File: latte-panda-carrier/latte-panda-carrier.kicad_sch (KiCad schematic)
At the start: 6 parts

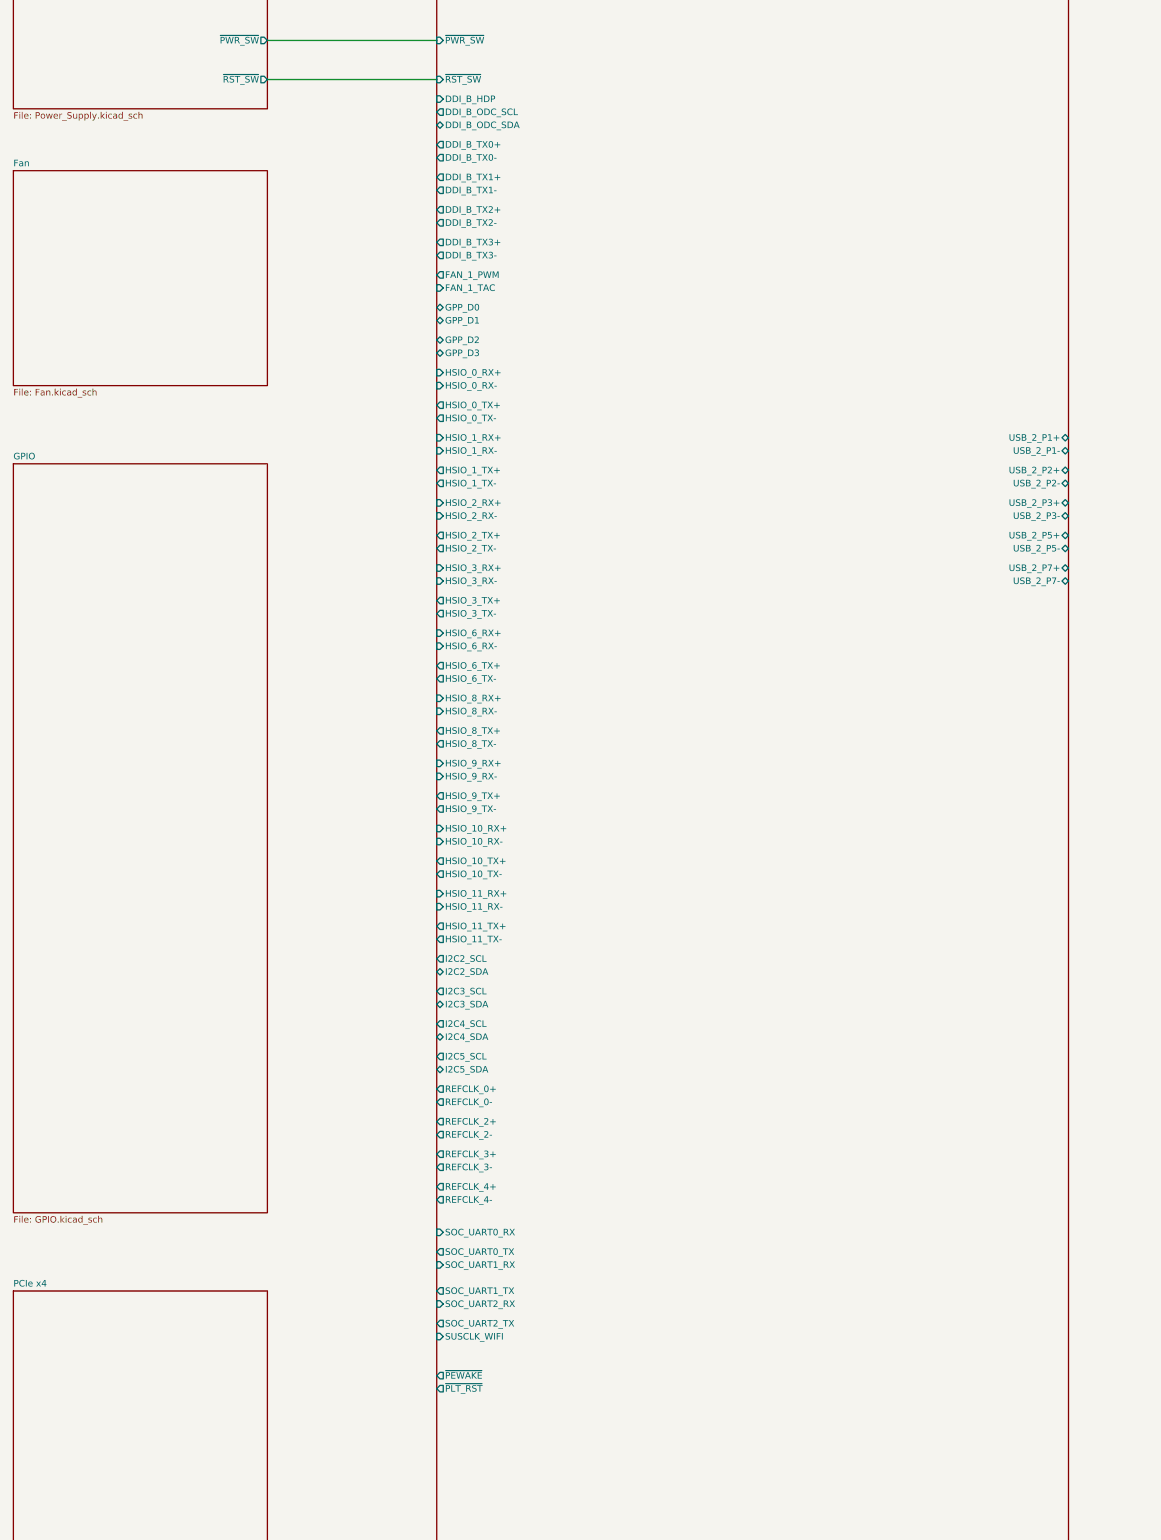
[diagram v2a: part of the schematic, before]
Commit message: 120.2
Wire CPU fan on root sheet and fix 2 power net name problems (+3V3 symbols
changed to +3.3V)
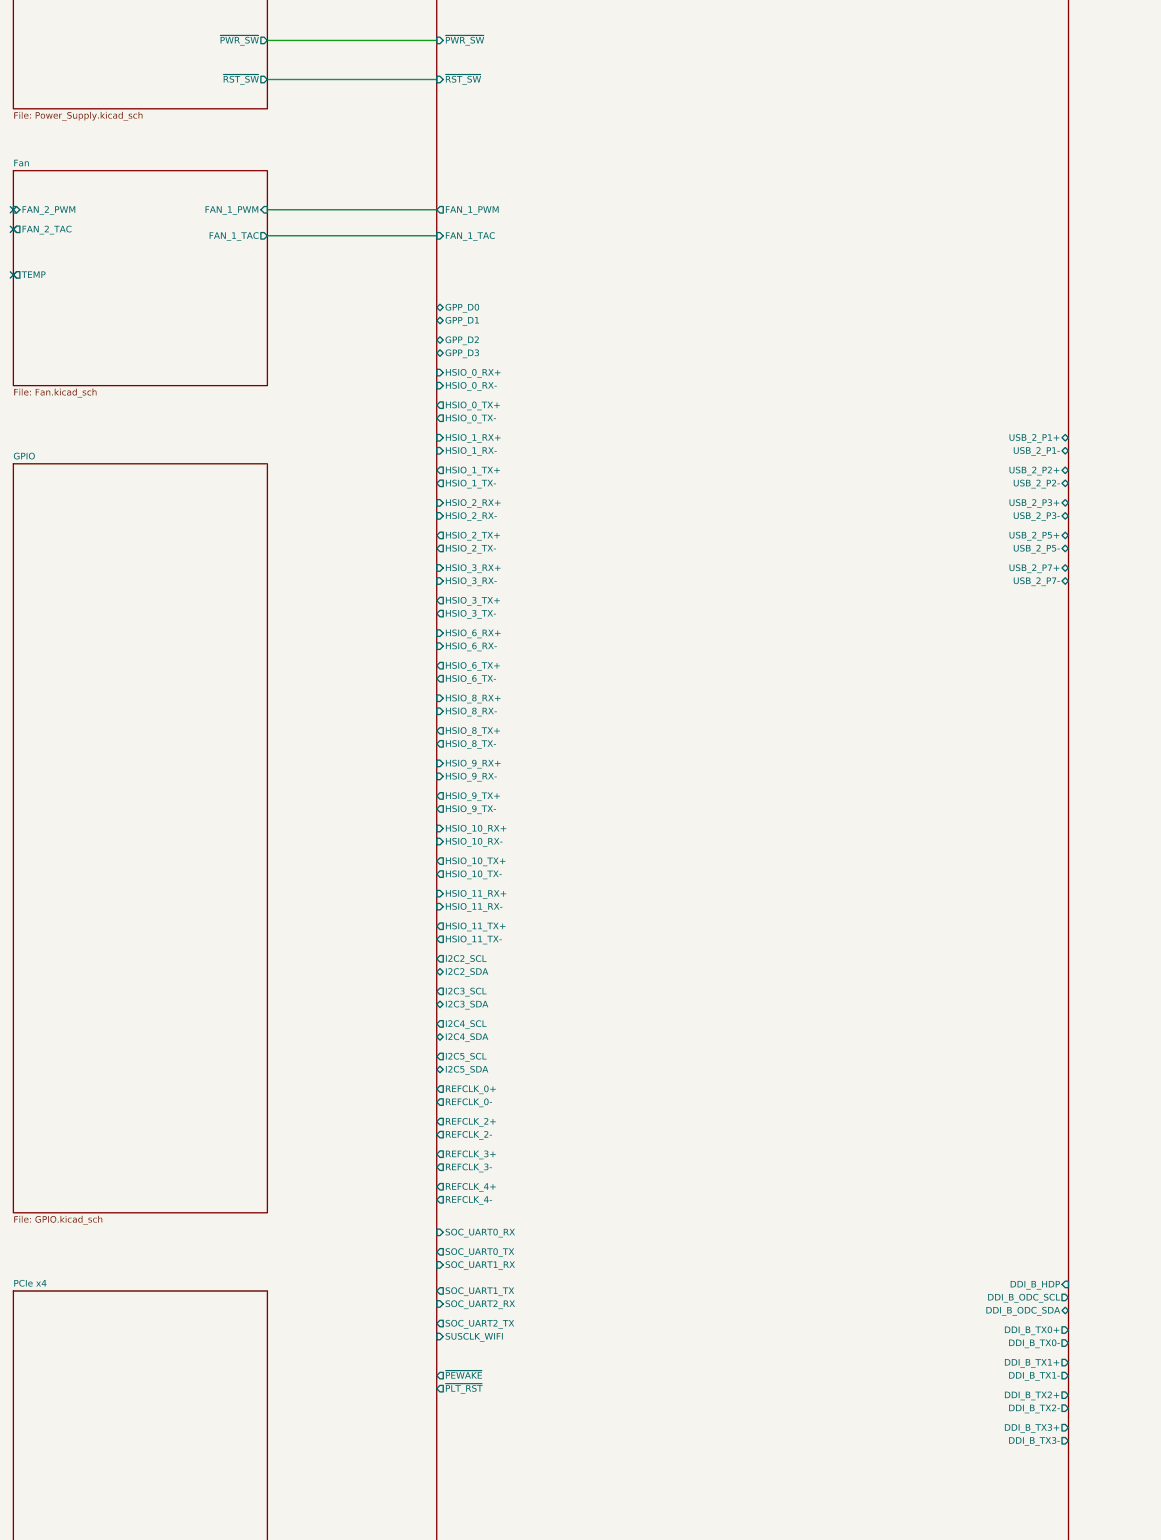
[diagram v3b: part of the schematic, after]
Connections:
- no-connect marks 0 -> 3
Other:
- sheet Fan ports: added FAN_1_PWM, FAN_1_TAC, FAN_2_PWM, FAN_2_TAC, TEMP; removed none
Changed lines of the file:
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@@
 		(rev "1.0")
+	)
+	(no_connect
+		(at 134.62 97.79)
+	)
+	(no_connect
+		(at 134.62 101.6)
+	)
+	(no_connect
+		(at 134.62 110.49)
 	)
 	(wire
@@
 		(pts
 			(xy 184.15 72.39) (xy 217.17 72.39)
+		)
+		(stroke
+			(width 0)
+			(type default)
+		)
+	)
+	(wire
+		(pts
+			(xy 184.15 97.79) (xy 217.17 97.79)
+		)
+		(stroke
+			(width 0)
+			(type default)
+		)
+	)
+	(wire
+		(pts
+			(xy 184.15 102.87) (xy 217.17 102.87)
 		)
 		(stroke
@@
 			)
 		)
+		(pin "FAN_1_PWM" input
+			(at 184.15 97.79 0)
+			(effects
+				(font
+					(size 1.27 1.27)
+				)
+				(justify right)
+			)
+		)
+		(pin "FAN_1_TAC" output
+			(at 184.15 102.87 0)
+			(effects
+				(font
+					(size 1.27 1.27)
+				)
+				(justify right)
+			)
+		)
+		(pin "FAN_2_PWM" input
+			(at 134.62 97.79 180)
+			(effects
+				(font
+					(size 1.27 1.27)
+				)
+				(justify left)
+			)
+		)
+		(pin "FAN_2_TAC" output
+			(at 134.62 101.6 180)
+			(effects
+				(font
+					(size 1.27 1.27)
+				)
+				(justify left)
+			)
+		)
+		(pin "TEMP" output
+			(at 134.62 110.49 180)
+			(effects
+				(font
+					(size 1.27 1.27)
+				)
+				(justify left)
+			)
+		)
 		(instances
 			(project "latte-panda-carrier"
@@
 		)
 		(pin "DDI_B_HDP" input
-			(at 217.17 76.2 180)
-			(effects
-				(font
-					(size 1.27 1.27)
-				)
-				(justify left)
+			(at 340.36 307.34 0)
+			(effects
+				(font
+					(size 1.27 1.27)
+				)
+				(justify right)
 			)
 		)
 		(pin "DDI_B_ODC_SCL" output
-			(at 217.17 78.74 180)
-			(effects
-				(font
-					(size 1.27 1.27)
-				)
-				(justify left)
+			(at 340.36 309.88 0)
+			(effects
+				(font
+					(size 1.27 1.27)
+				)
+				(justify right)
 			)
 		)
 		(pin "DDI_B_ODC_SDA" bidirectional
-			(at 217.17 81.28 180)
-			(effects
-				(font
-					(size 1.27 1.27)
-				)
-				(justify left)
+			(at 340.36 312.42 0)
+			(effects
+				(font
+					(size 1.27 1.27)
+				)
+				(justify right)
 			)
 		)
 		(pin "DDI_B_TX0+" output
-			(at 217.17 85.09 180)
-			(effects
-				(font
-					(size 1.27 1.27)
-				)
-				(justify left)
+			(at 340.36 316.23 0)
+			(effects
+				(font
+					(size 1.27 1.27)
+				)
+				(justify right)
 			)
 		)
 		(pin "DDI_B_TX0-" output
-			(at 217.17 87.63 180)
-			(effects
-				(font
-					(size 1.27 1.27)
-				)
-				(justify left)
+			(at 340.36 318.77 0)
+			(effects
+				(font
+					(size 1.27 1.27)
+				)
+				(justify right)
 			)
 		)
 		(pin "DDI_B_TX1+" output
-			(at 217.17 91.44 180)
-			(effects
-				(font
-					(size 1.27 1.27)
-				)
-				(justify left)
+			(at 340.36 322.58 0)
+			(effects
+				(font
+					(size 1.27 1.27)
+				)
+				(justify right)
 			)
 		)
 		(pin "DDI_B_TX1-" output
-			(at 217.17 93.98 180)
-			(effects
-				(font
-					(size 1.27 1.27)
-				)
-				(justify left)
+			(at 340.36 325.12 0)
+			(effects
+				(font
+					(size 1.27 1.27)
+				)
+				(justify right)
 			)
 		)
 		(pin "DDI_B_TX2+" output
+			(at 340.36 328.93 0)
+			(effects
+				(font
+					(size 1.27 1.27)
+				)
+				(justify right)
+			)
+		)
+		(pin "DDI_B_TX2-" output
+			(at 340.36 331.47 0)
+			(effects
+				(font
+					(size 1.27 1.27)
+				)
+				(justify right)
+			)
+		)
+		(pin "DDI_B_TX3+" output
+			(at 340.36 335.28 0)
+			(effects
+				(font
+					(size 1.27 1.27)
+				)
+				(justify right)
+			)
+		)
+		(pin "DDI_B_TX3-" output
+			(at 340.36 337.82 0)
+			(effects
+				(font
+					(size 1.27 1.27)
+				)
+				(justify right)
+			)
+		)
+		(pin "FAN_1_PWM" output
 			(at 217.17 97.79 180)
 			(effects
@@
 			)
 		)
-		(pin "DDI_B_TX2-" output
-			(at 217.17 100.33 180)
-			(effects
-				(font
-					(size 1.27 1.27)
-				)
-				(justify left)
-			)
-		)
-		(pin "DDI_B_TX3+" output
-			(at 217.17 104.14 180)
-			(effects
-				(font
-					(size 1.27 1.27)
-				)
-				(justify left)
-			)
-		)
-		(pin "DDI_B_TX3-" output
-			(at 217.17 106.68 180)
-			(effects
-				(font
-					(size 1.27 1.27)
-				)
-				(justify left)
-			)
-		)
-		(pin "FAN_1_PWM" output
-			(at 217.17 110.49 180)
-			(effects
-				(font
-					(size 1.27 1.27)
-				)
-				(justify left)
-			)
-		)
 		(pin "FAN_1_TAC" input
-			(at 217.17 113.03 180)
-			(effects
-				(font
+			(at 217.17 102.87 180)
+			(effects
+				(font

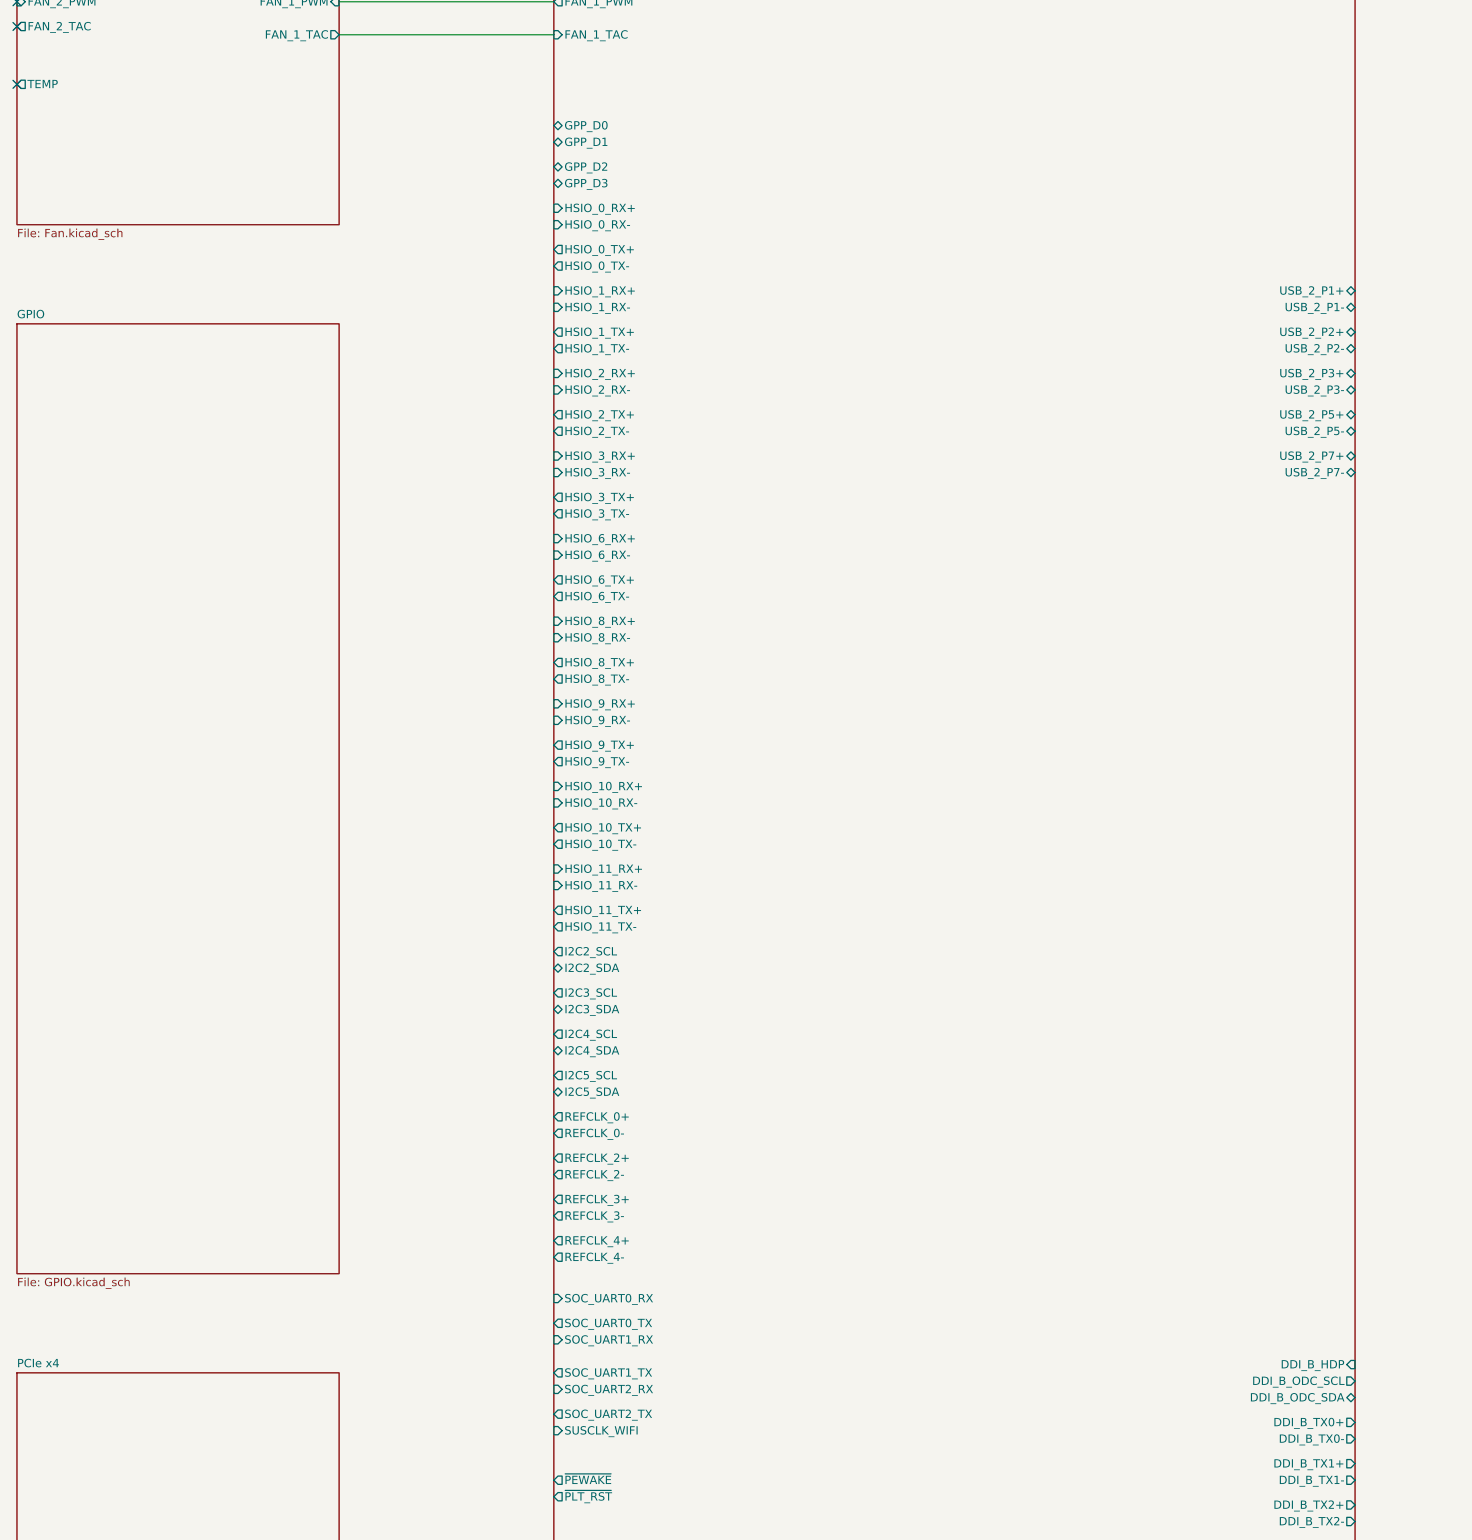
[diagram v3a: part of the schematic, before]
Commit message: 130.2
Add connections to root sheet for GPIO, I2C and UART.
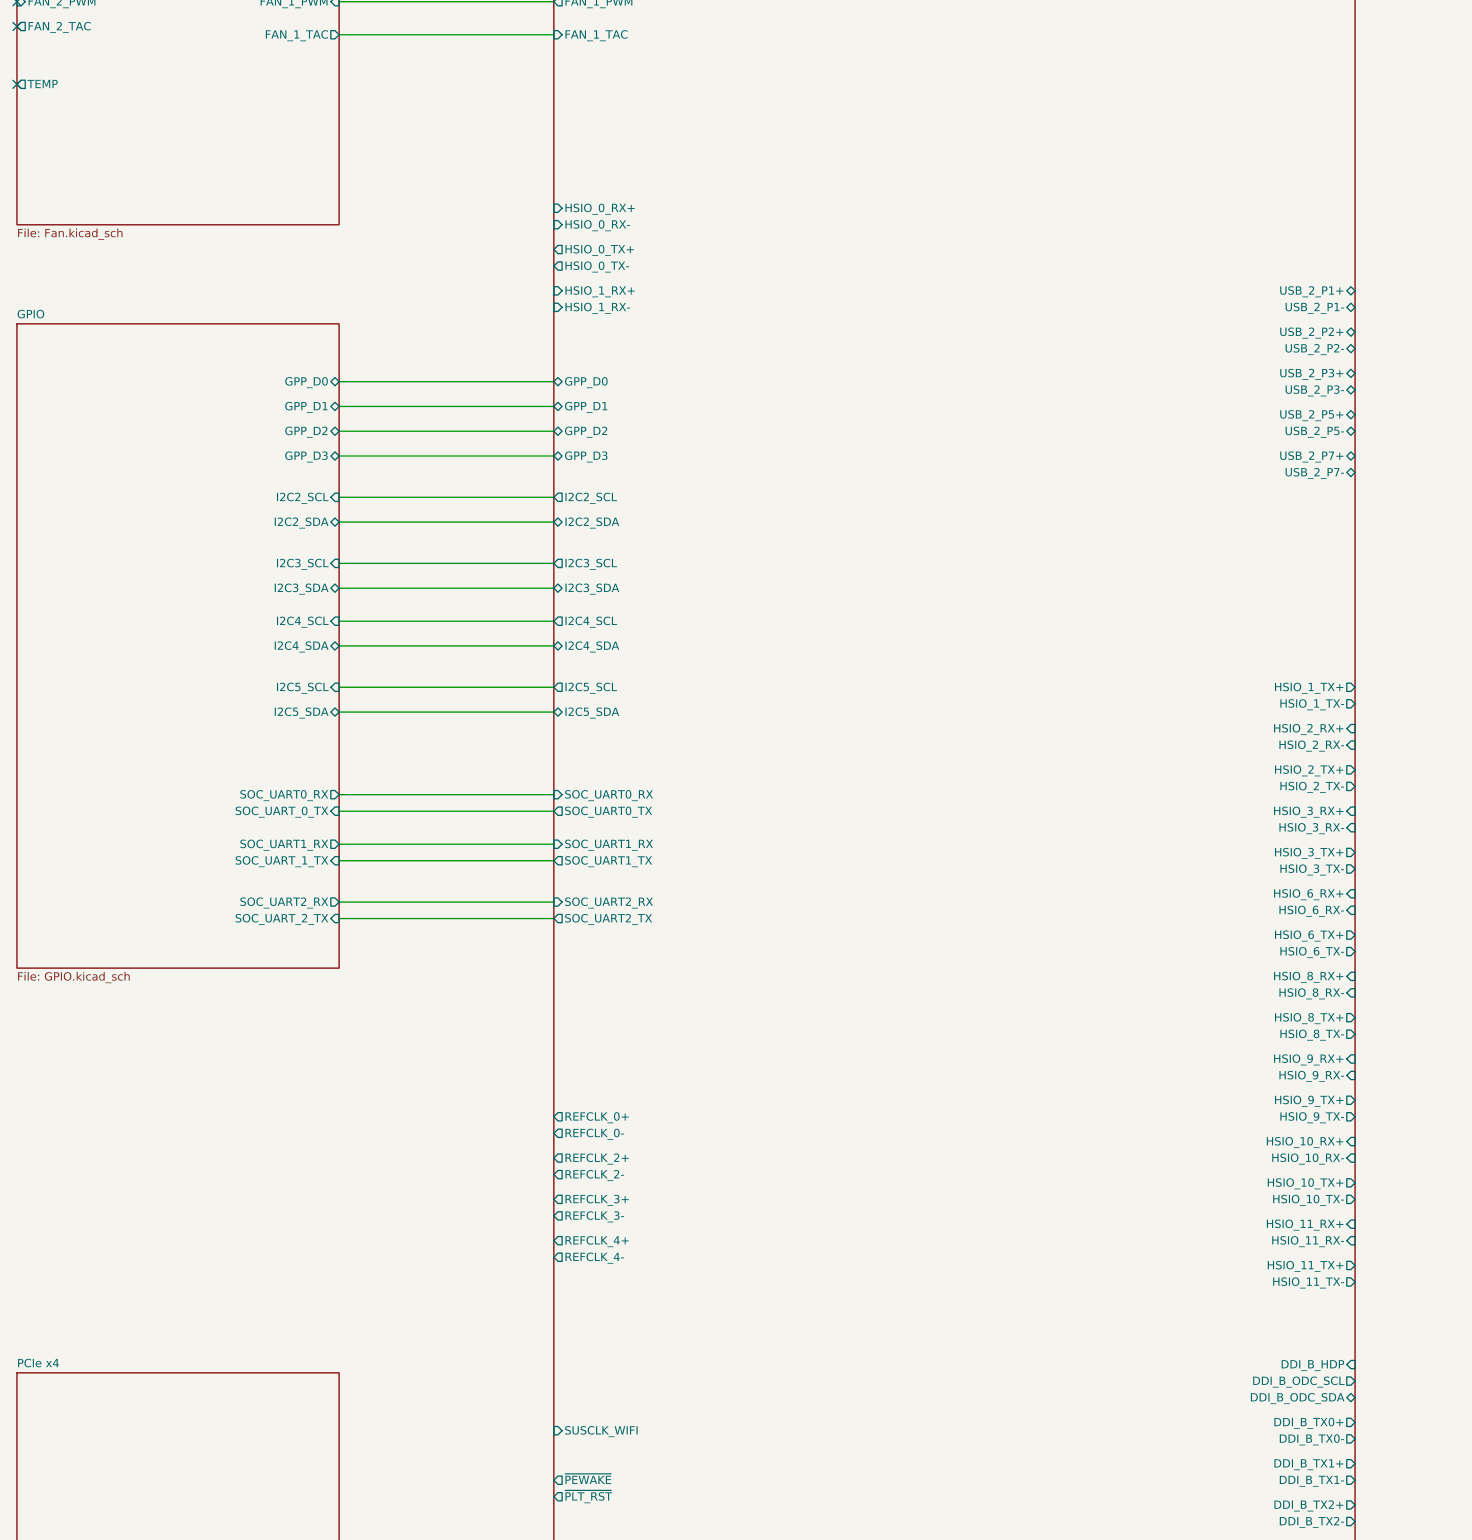
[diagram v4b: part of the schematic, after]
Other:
- sheet GPIO ports: added GPP_D0, GPP_D1, GPP_D2, GPP_D3, I2C2_SCL, I2C2_SDA, I2C3_SCL, I2C3_SDA, I2C4_SCL, I2C4_SDA, I2C5_SCL, I2C5_SDA, SOC_UART0_RX, SOC_UART1_RX, SOC_UART2_RX, SOC_UART_0_TX, SOC_UART_1_TX, SOC_UART_2_TX; removed none
